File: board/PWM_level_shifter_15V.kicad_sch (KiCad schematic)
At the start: 7 parts, among them U3 H11L1, U4 H11L1, U5 H11L1, U6 H11L1, U7 H11L1, U8 H11L1, U9 4049

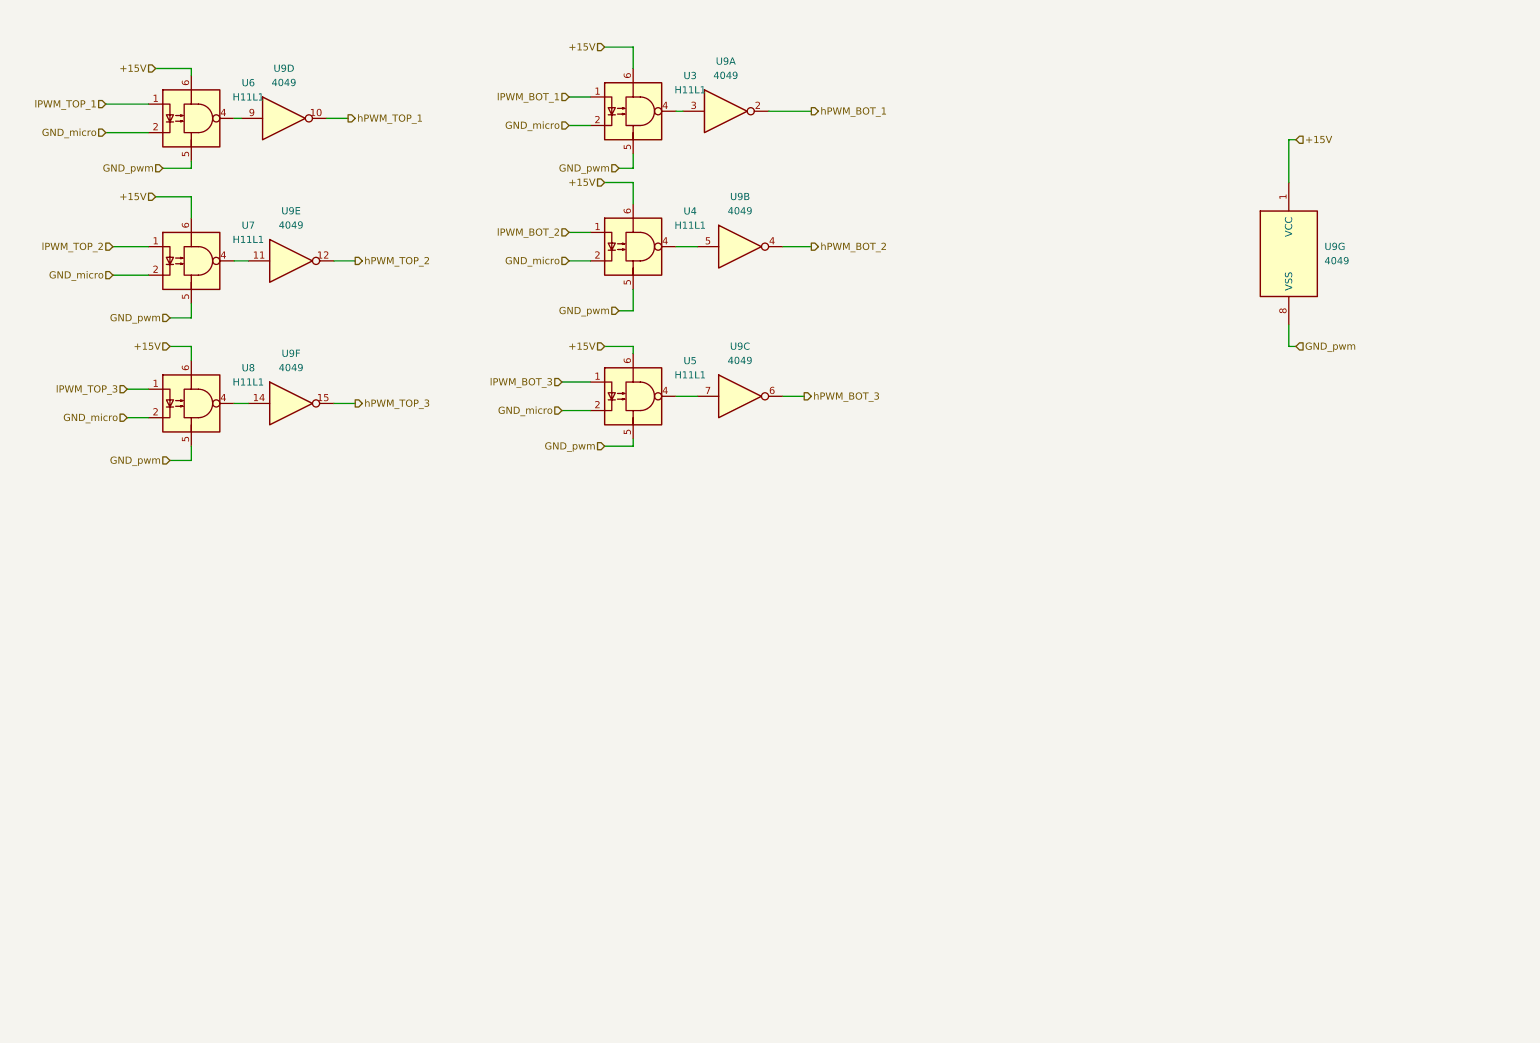
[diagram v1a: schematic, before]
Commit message: Schematic changes: Complete PWM voltage level shifter
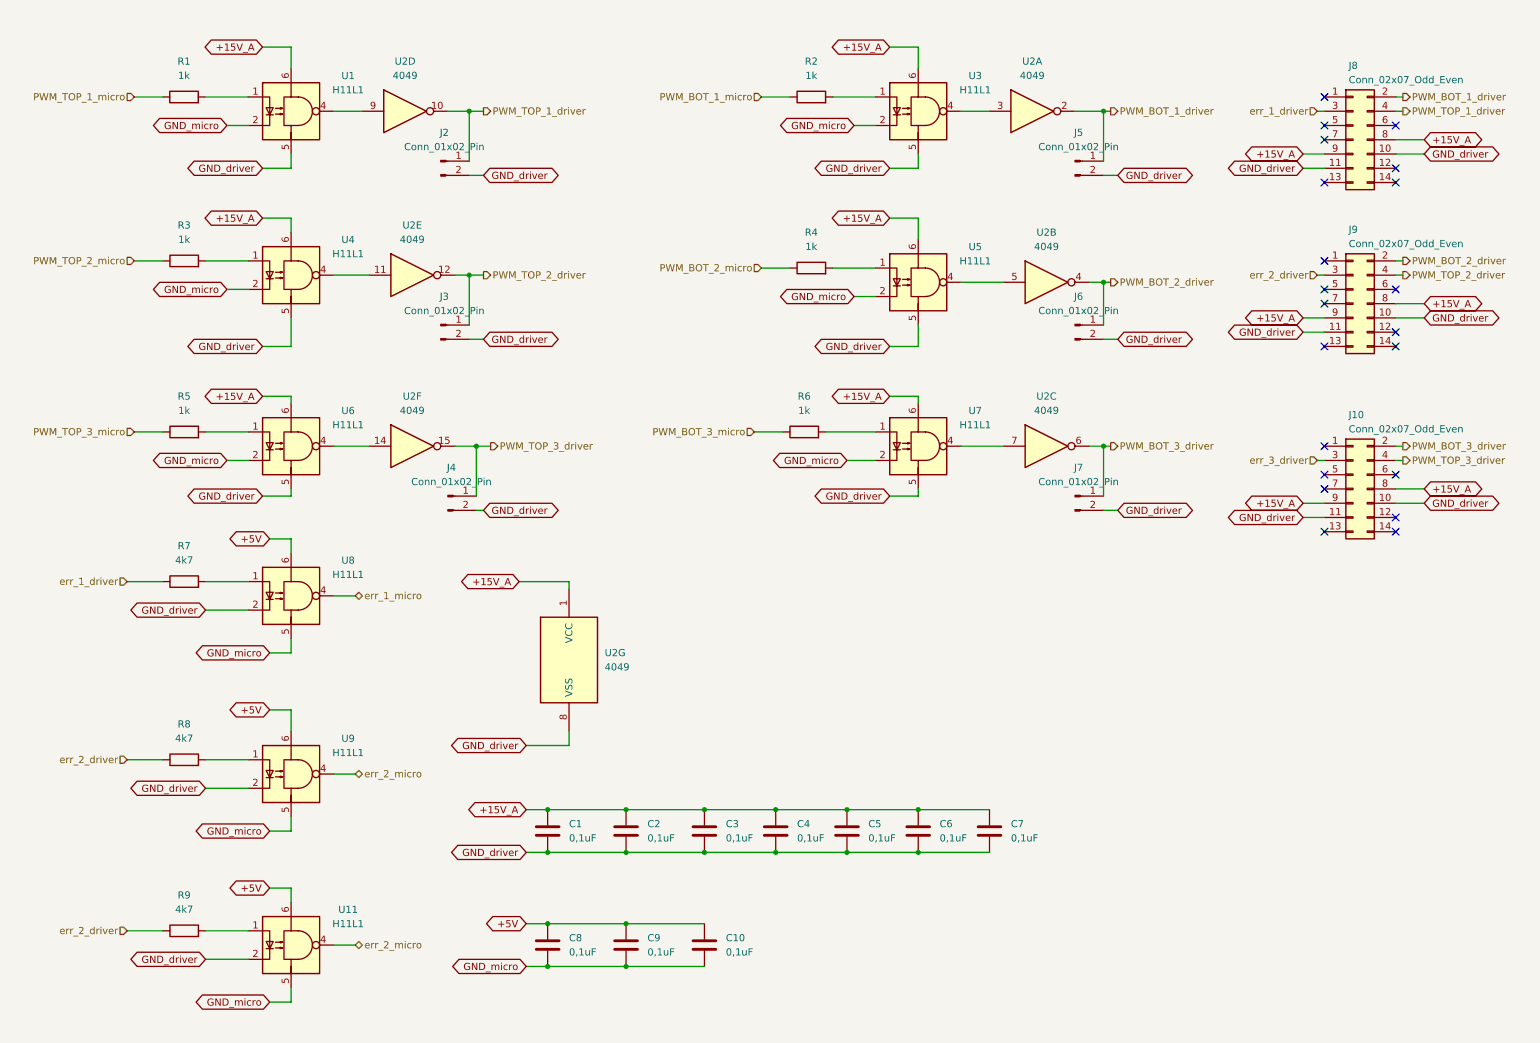
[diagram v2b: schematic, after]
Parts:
- added C1, C10, C2, C3, C4, C5, C6, C7, C8, C9: 0,1uF, symbol Device:C
- added J10, J8, J9: Conn_02x07_Odd_Even, symbol Connector_Generic:Conn_02x07_Odd_Even
- added J2, J3, J4, J5, J6, J7: Conn_01x02_Pin, symbol Connector:Conn_01x02_Pin
- added R1, R2, R3, R4, R5, R6: 1k, symbol Device:R
- added R7, R8, R9: 4k7, symbol Device:R
- added U11, U8, U9: H11L1, symbol Isolator:H11L1
- renumbered U6 to U1, U9 to U2, U7 to U4, U4 to U5, U8 to U6, U5 to U7
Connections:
- net GND_micro: now also C10.2, C8.2, C9.2, U11.5, U8.5, U9.5
- net +15V renamed +15V_A
- net +15V_A: now also C1.1, C2.1, C3.1, C4.1, C5.1, C6.1, C7.1, J10.8 (Pin_8), J10.9 (Pin_9), J8.8 (Pin_8), J8.9 (Pin_9), J9.8 (Pin_8), J9.9 (Pin_9)
- net GND_pwm renamed GND_driver
- net GND_driver: now also C1.2, C2.2, C3.2, C4.2, C5.2, C6.2, C7.2, J10.10 (Pin_10), J10.11 (Pin_11), J2.2 (Pin_2), J3.2 (Pin_2), J4.2 (Pin_2), J5.2 (Pin_2), J6.2 (Pin_2), J7.2 (Pin_2), J8.10 (Pin_10), J8.11 (Pin_11), J9.10 (Pin_10), J9.11 (Pin_11), U11.2, U8.2, U9.2
- net hPWM_BOT_1 renamed PWM_BOT_1_driver
- net PWM_BOT_1_driver: now also J5.1 (Pin_1), J8.2 (Pin_2)
- net hPWM_BOT_2 renamed PWM_BOT_2_driver
- net PWM_BOT_2_driver: now also J6.1 (Pin_1), J9.2 (Pin_2)
- net hPWM_BOT_3 renamed PWM_BOT_3_driver
- net PWM_BOT_3_driver: now also J10.2 (Pin_2), J7.1 (Pin_1)
- net hPWM_TOP_1 renamed PWM_TOP_1_driver
- net PWM_TOP_1_driver: now also J2.1 (Pin_1), J8.4 (Pin_4)
- net hPWM_TOP_2 renamed PWM_TOP_2_driver
- net PWM_TOP_2_driver: now also J3.1 (Pin_1), J9.4 (Pin_4)
- net hPWM_TOP_3 renamed PWM_TOP_3_driver
- net PWM_TOP_3_driver: now also J10.4 (Pin_4), J4.1 (Pin_1)
- net lPWM_BOT_1: no longer names the net of U3.1
- net lPWM_BOT_1: now also R2.2
- net lPWM_BOT_2: no longer names the net of U5.1
- net lPWM_BOT_2: now also R4.2
- net lPWM_BOT_3: no longer names the net of U7.1
- net lPWM_BOT_3: now also R6.2
- net lPWM_TOP_1: no longer names the net of U1.1
- net lPWM_TOP_1: now also R1.2
- net lPWM_TOP_2: no longer names the net of U4.1
- net lPWM_TOP_2: now also R3.2
- net lPWM_TOP_3: no longer names the net of U6.1
- net lPWM_TOP_3: now also R5.2
- new net: R8.2, U9.1
- new net: R9.2, U11.1
- new net: R7.2, U8.1
- new net +5V: C10.1, C8.1, C9.1, U11.6, U8.6, U9.6
- new net PWM_BOT_1_micro: R2.1
- new net PWM_BOT_2_micro: R4.1
- new net PWM_BOT_3_micro: R6.1
- new net PWM_TOP_1_micro: R1.1
- new net PWM_TOP_2_micro: R3.1
- new net PWM_TOP_3_micro: R5.1
- new net err_1_driver: J8.3 (Pin_3), R7.1
- new net err_1_micro: U8.4
- new net err_2_driver: J9.3 (Pin_3), R8.1, R9.1
- new net err_2_micro: U11.4, U9.4
- new net err_3_driver: J10.3 (Pin_3)
- no-connect marks 0 -> 21
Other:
- moved on the sheet: U1, U2A, U2B, U2C, U2D, U2E, U2F, U2G, U3, U4, U5, U6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

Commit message: Schematic changes: Fix optocoupler output, fix resistor values
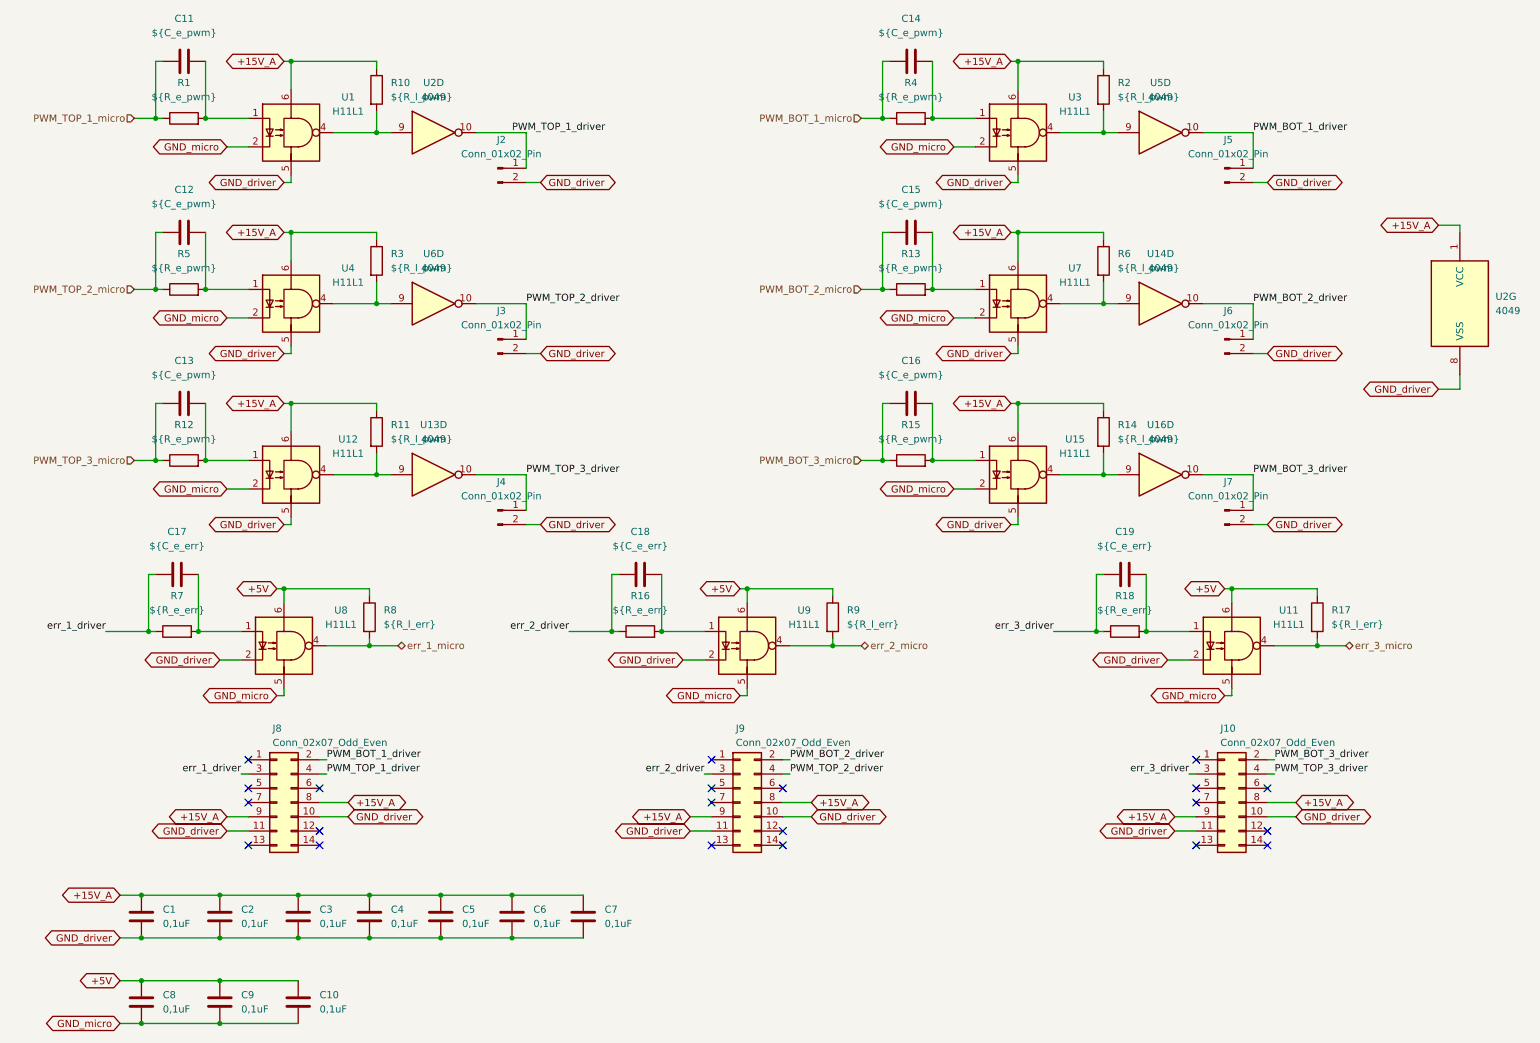
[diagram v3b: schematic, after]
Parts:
- removed unit 2 of U2
- removed unit 5 of U2
- removed unit 3 of U2
- removed unit 6 of U2
- removed unit 1 of U2
- removed U5, U6: H11L1, symbol Isolator:H11L1
- added C11, C12, C13, C14, C15, C16: ${C_e_pwm}, symbol Device:C
- added C17, C18, C19: ${C_e_err}, symbol Device:C
- added R10, R11, R14: ${R_l_pwm}, symbol Device:R
- added R12, R13, R15: ${R_e_pwm}, symbol Device:R
- added R16, R18: ${R_e_err}, symbol Device:R
- added R17: ${R_l_err}, symbol Device:R
- added U12, U15: H11L1, symbol Isolator:H11L1
- added U13, U14, U16, U5, U6: 4049, symbol 4xxx:4049
- R1, R4, R5: value 1k -> ${R_e_pwm}
- R2, R3, R6: value 1k -> ${R_l_pwm}
- R7: value 4k7 -> ${R_e_err}
- R8, R9: value 4k7 -> ${R_l_err}
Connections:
- net +15V_A: now also R2.1, R3.1, R6.1, R10.1, R11.1, R14.1, U12.6, U15.6
- net +5V: now also R8.1, R9.1, R17.1
- net GND_driver: now also U12.5, U15.5
- net GND_micro: now also U12.2, U15.2
- net PWM_BOT_1_driver: now also U5.10
- net PWM_BOT_1_micro: now also R4.1, C14.1; no longer R2.1
- net PWM_BOT_2_driver: now also U14.10
- net PWM_BOT_2_micro: now also C15.1, R13.1; no longer R4.1
- net PWM_BOT_3_driver: now also U16.10
- net PWM_BOT_3_micro: now also C16.1, R15.1; no longer R6.1
- net PWM_TOP_1_micro: now also C11.1
- net PWM_TOP_2_driver: now also U6.10
- net PWM_TOP_2_micro: now also R5.1, C12.1; no longer R3.1
- net PWM_TOP_3_driver: now also U13.10
- net PWM_TOP_3_micro: now also C13.1, R12.1; no longer R5.1
- net err_1_driver: now also C17.1
- net err_1_micro: now also R8.2
- net err_2_driver: now also C18.1, R16.1; no longer R8.1, R9.1
- net err_2_micro: now also R9.2; no longer U11.4
- net err_3_driver: now also C19.1, R18.1
- net at U4.4: now also R3.2, U6.9
- net at U9.1: now also C18.2, R16.2; no longer R8.2
- net at U11.1: now also C19.2, R18.2; no longer R9.2
- net at U4.1: now also R5.2, C12.2; no longer R3.2
- net at U7.4: now also R6.2, U14.9
- net at U1.4, U2.9: now also R10.2
- net at R4.2: now also U3.1, C14.2
- net at U7.1: now also C15.2, R13.2; no longer R6.2
- net at R2.2: now also U3.4, U5.9; no longer U3.1
- net at R1.2, U1.1: now also C11.2
- net at R7.2, U8.1: now also C17.2
- new net: C13.2, R12.2, U12.1
- new net: R14.2, U15.4, U16.9
- new net: R11.2, U12.4, U13.9
- new net: C16.2, R15.2, U15.1
- new net err_3_micro: R17.2, U11.4
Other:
- moved on the sheet: C1, C10, C2, C3, C4, C5, C6, C7, C8, C9, J10, J2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

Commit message: Schematic changes and board creation
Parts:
- removed C1, C10, C2, C3, C4, C5, C6, C7, C8, C9: 0,1uF, symbol Device:C
- removed C11, C12, C13, C14, C15, C16: ${C_e_pwm}, symbol Device:C
- removed C17, C18, C19: ${C_e_err}, symbol Device:C
- removed J10, J8, J9: Conn_02x07_Odd_Even, symbol Connector_Generic:Conn_02x07_Odd_Even
- removed J2, J3, J4, J5, J6, J7: Conn_01x02_Pin, symbol Connector:Conn_01x02_Pin
- removed R1, R12, R13, R15, R4, R5: ${R_e_pwm}, symbol Device:R
- removed R10, R11, R14, R2, R3, R6: ${R_l_pwm}, symbol Device:R
- removed R16, R18, R7: ${R_e_err}, symbol Device:R
- removed R17, R8, R9: ${R_l_err}, symbol Device:R
- removed U1, U11, U12, U15, U3, U4, U7, U8, U9: H11L1, symbol Isolator:H11L1
- removed U13, U14, U16, U2, U5, U6: 4049, symbol 4xxx:4049
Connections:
- no-connect marks 21 -> 0
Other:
- added sheet Conectores - PWM e erro (conn_driver.kicad_sch)
- added sheet Conectores - PWM e erro1 (conn_driver.kicad_sch)
- added sheet Conectores - PWM e erro2 (conn_driver.kicad_sch)
